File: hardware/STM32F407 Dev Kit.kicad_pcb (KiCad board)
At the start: 4 copper layers, 65.2 x 58.4 mm, 153 parts, among them J1 GMSB0531112YEU, J10 Conn_01x04, J11 TBC 2.54mm 10A, J12 IMP34DT05, J2 Conn_01x06, J3 RJMG1S8008101BR, J4 B2B-XH-A(LF)(SN), J5 Conn_01x04, J7 SJ-3524-SMT, J8 GMSB0531112YEU, J9 Conn_01x04, SW1 SW TACT-SPST, SW2 SW TACT-SPST, SW3 SW TACT-SPST, U1 STM32F103CBT6, U2 DP83826IRHBR, U3 DRV8701ERGET, U4 DMHT6016LFJ-13, U5 ADS122C04IPW, U6 CS43L22, U7 STM32F407VGT6, U8 AP63203WU, U9 XC6206P182MR, Y1 ABM8G-8.000MHZ-18-D2Y-T, Y2 ABM8G-25.000MHZ-9-B4Y-T, Y3 ABM8G-8.000MHZ-18-D2Y-T

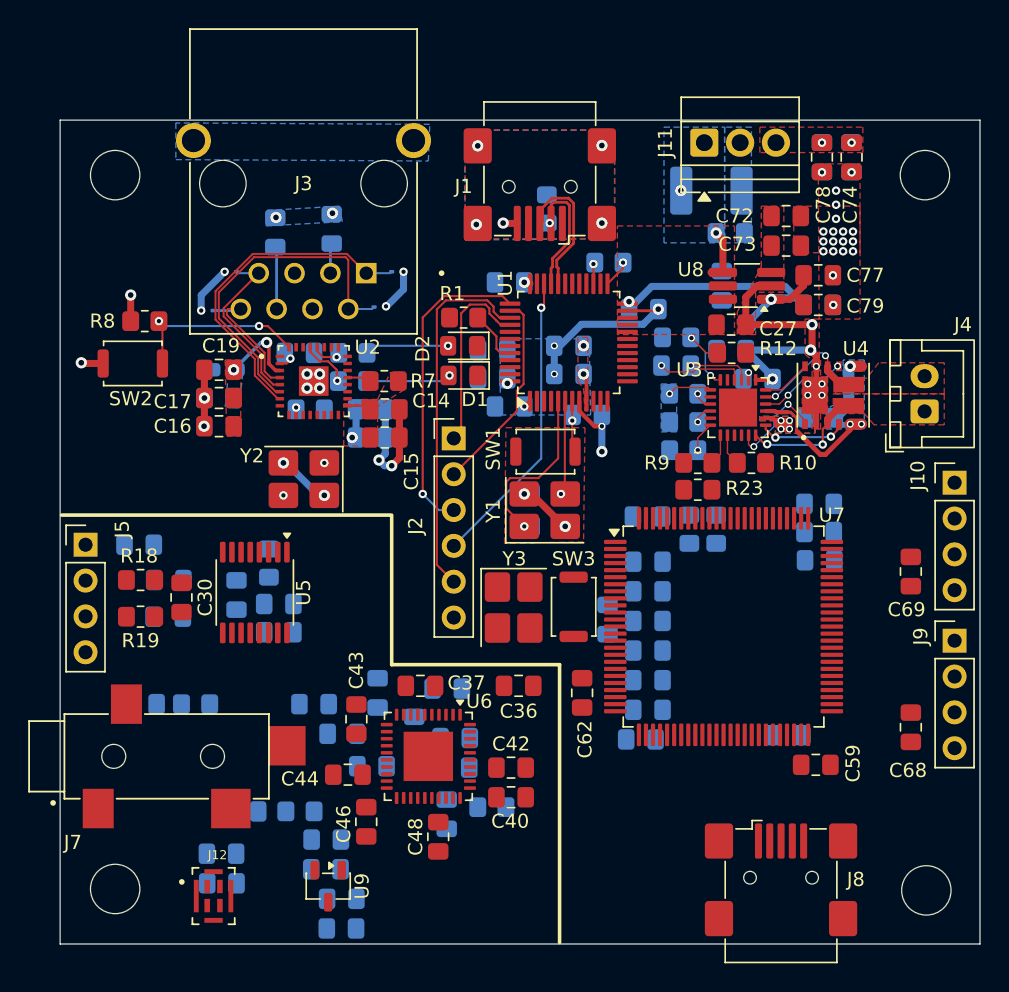
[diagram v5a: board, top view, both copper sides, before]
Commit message: Route Audio and ADC section
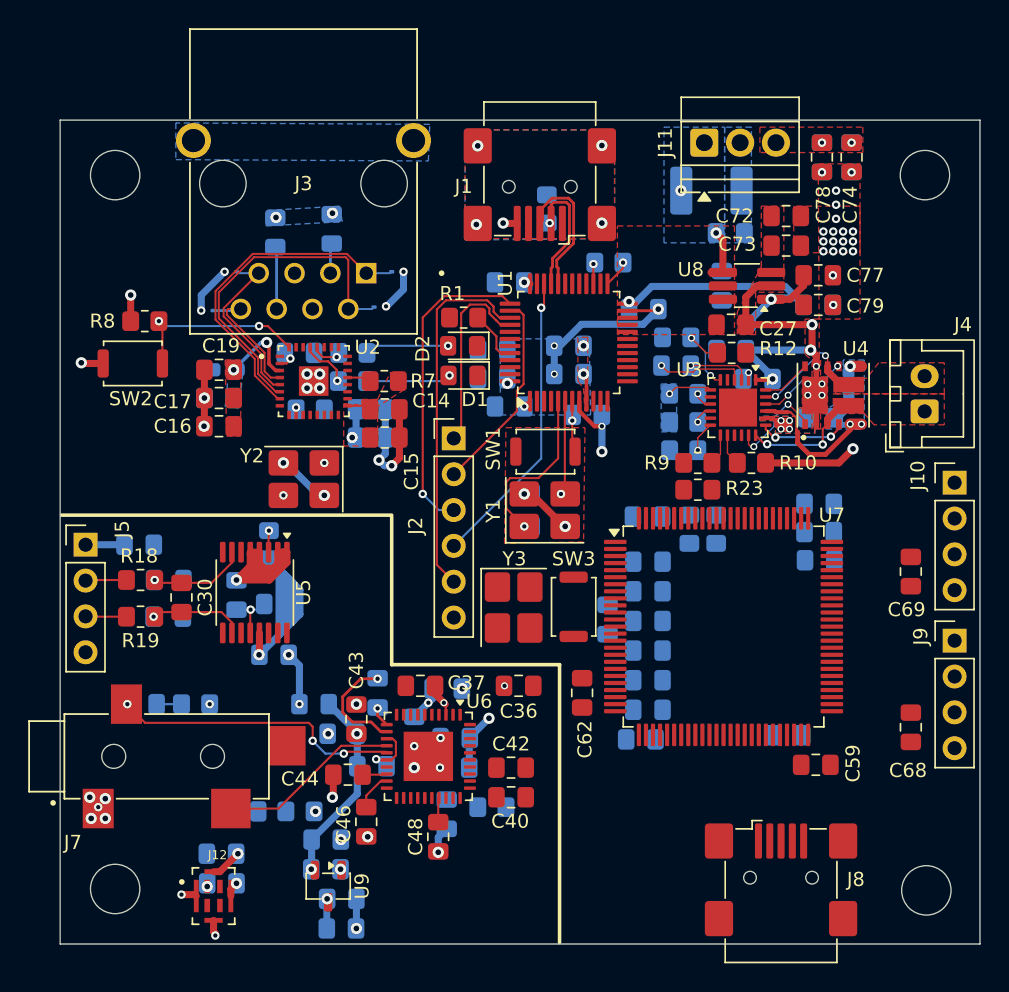
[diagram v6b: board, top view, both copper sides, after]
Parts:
- moved C28 1.64 mm to (165.2, 87.9)
- moved R17 1.30 mm to (164.8, 80.1)
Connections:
- U7 pad 65: MIC_CLK -> unconnected-(U7-PC8-Pad65)
- U7 pad 66: unconnected-(U7-PC9-Pad66) -> MIC_DOUT
- U7 pad 78: unconnected-(U7-PC10-Pad78) -> MIC_CLK
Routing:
- net GND: track 61.8 -> 111.9 mm, vias 54 -> 83
- net +3V3: track 31.9 -> 72.3 mm, vias 9 -> 15
- net /[7] - DAC & Mic/HP_LINE_OUTA: track 0.00 -> 20.6 mm, vias 0 -> 3
- net +1V8: track 0.00 -> 13.9 mm, vias 0 -> 2
- net /[7] - DAC & Mic/HP_LINE_OUTB: track 0.00 -> 12.9 mm
- net /[7] - DAC & Mic/FLYP: track 0.00 -> 7.84 mm, vias 0 -> 1
- net /[6] - ADC/AIN2: track 0.00 -> 6.93 mm, vias 0 -> 1
- net /[6] - ADC/AIN1: track 0.00 -> 6.84 mm, vias 0 -> 1
- net /[7] - DAC & Mic/VA: track 0.00 -> 4.20 mm, vias 0 -> 1
- net Net-(U5-AVDD): track 0.00 -> 3.79 mm, vias 0 -> 1
- net /[6] - ADC/SENSOR_PIN2: track 0.00 -> 2.92 mm
- net /[6] - ADC/SENSOR_PIN1: track 0.00 -> 2.91 mm
- net Net-(U6-VQ): track 0.00 -> 2.70 mm
- net Net-(C51-Pad1): track 0.00 -> 1.76 mm
- net Net-(U6-FILT+): track 0.00 -> 1.73 mm
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
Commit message: Route STM32F407 section
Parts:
- moved C61 1.00 mm to (204.8, 81.2)
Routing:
- net GND: track 111.9 -> 139.0 mm, vias 83 -> 100
- net /[8] - STM32F407/F407_USB_N: track 0.00 -> 22.0 mm
- net /[8] - STM32F407/F407_USB_P: track 0.00 -> 21.8 mm
- net +3V3: track 72.3 -> 92.6 mm, vias 15 -> 20
- net /[8] - STM32F407/CAN_TX: track 0.00 -> 14.7 mm
- net /[8] - STM32F407/CAN_RX: track 0.00 -> 14.3 mm
- net /[8] - STM32F407/UART_TX: track 0.00 -> 11.2 mm
- net /[8] - STM32F407/UART_RX: track 0.00 -> 10.4 mm
- net /[8] - STM32F407/F407_OSC_IN: track 0.00 -> 9.30 mm, vias 0 -> 1
- net /[8] - STM32F407/F407_VDDA: track 0.00 -> 7.19 mm, vias 0 -> 2
- net /[8] - STM32F407/F407_OSC_OUT: track 0.00 -> 6.23 mm, vias 0 -> 1
- net /[8] - STM32F407/SDA: track 0.00 -> 5.37 mm, vias 0 -> 1
- net /[8] - STM32F407/SCL: track 0.00 -> 4.03 mm, vias 0 -> 1
- net F407_NTRST: track 0.00 -> 3.97 mm, vias 0 -> 1
- net /[8] - STM32F407/F407_VCAP1: track 0.00 -> 2.12 mm
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- added copper zone on B.Cu, net /[8] - STM32F407/F407_VDDA
- added copper zone on F.Cu, net /[8] - STM32F407/F407_VDDA
